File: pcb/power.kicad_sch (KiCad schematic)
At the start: 18 parts, among them J5 9V Battery, J6 9V Barrel Female, U3 MCP1700T-3302E/TT, U4 TPS54302

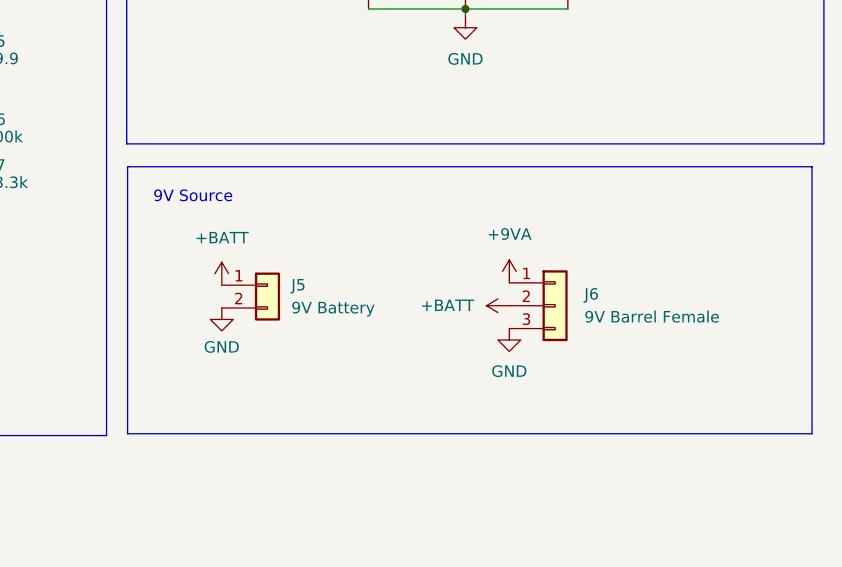
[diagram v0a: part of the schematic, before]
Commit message: Added filtering cap to 9V barrel
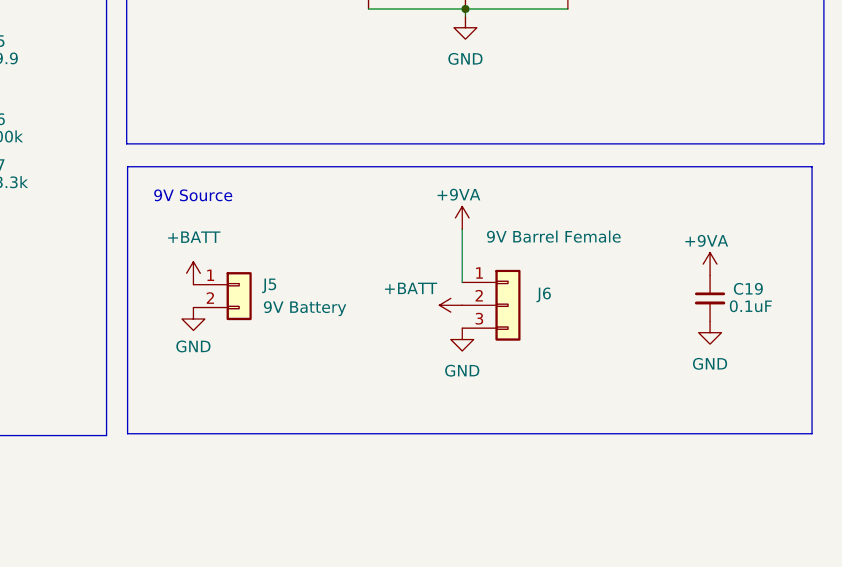
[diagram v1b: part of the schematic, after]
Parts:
- added C19: 0.1uF, symbol Device:C_Small
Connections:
- net +9VA: now also C19.1
- net GND: now also C19.2
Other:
- moved on the sheet: J5, J6

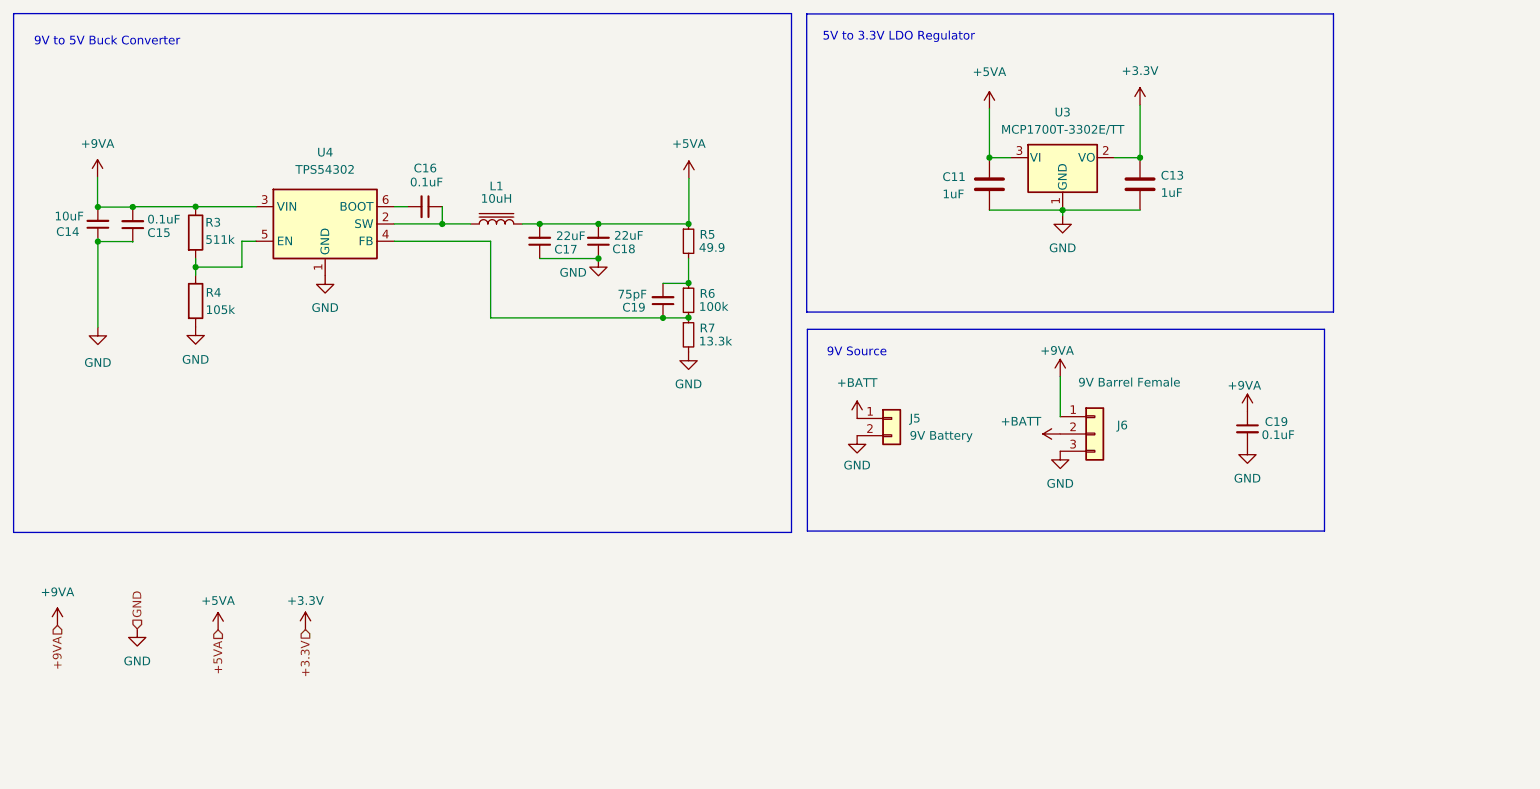
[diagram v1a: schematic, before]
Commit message: Removed power hierarchy labels
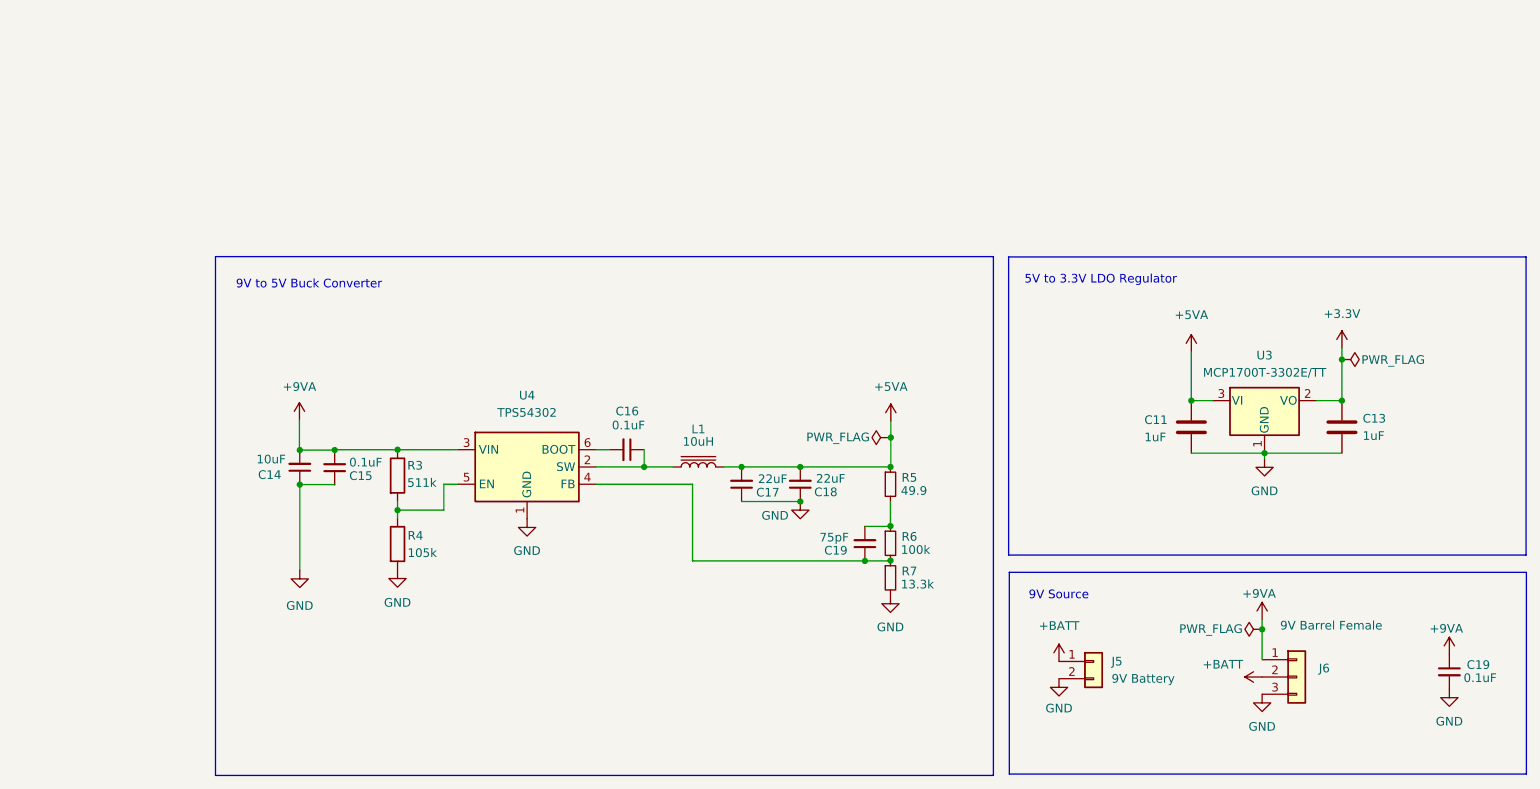
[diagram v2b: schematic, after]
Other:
- moved on the sheet: C11, C13, C14, C15, C16, C17, C18, C19, J5, J6, L1, R3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

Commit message: Reordered components
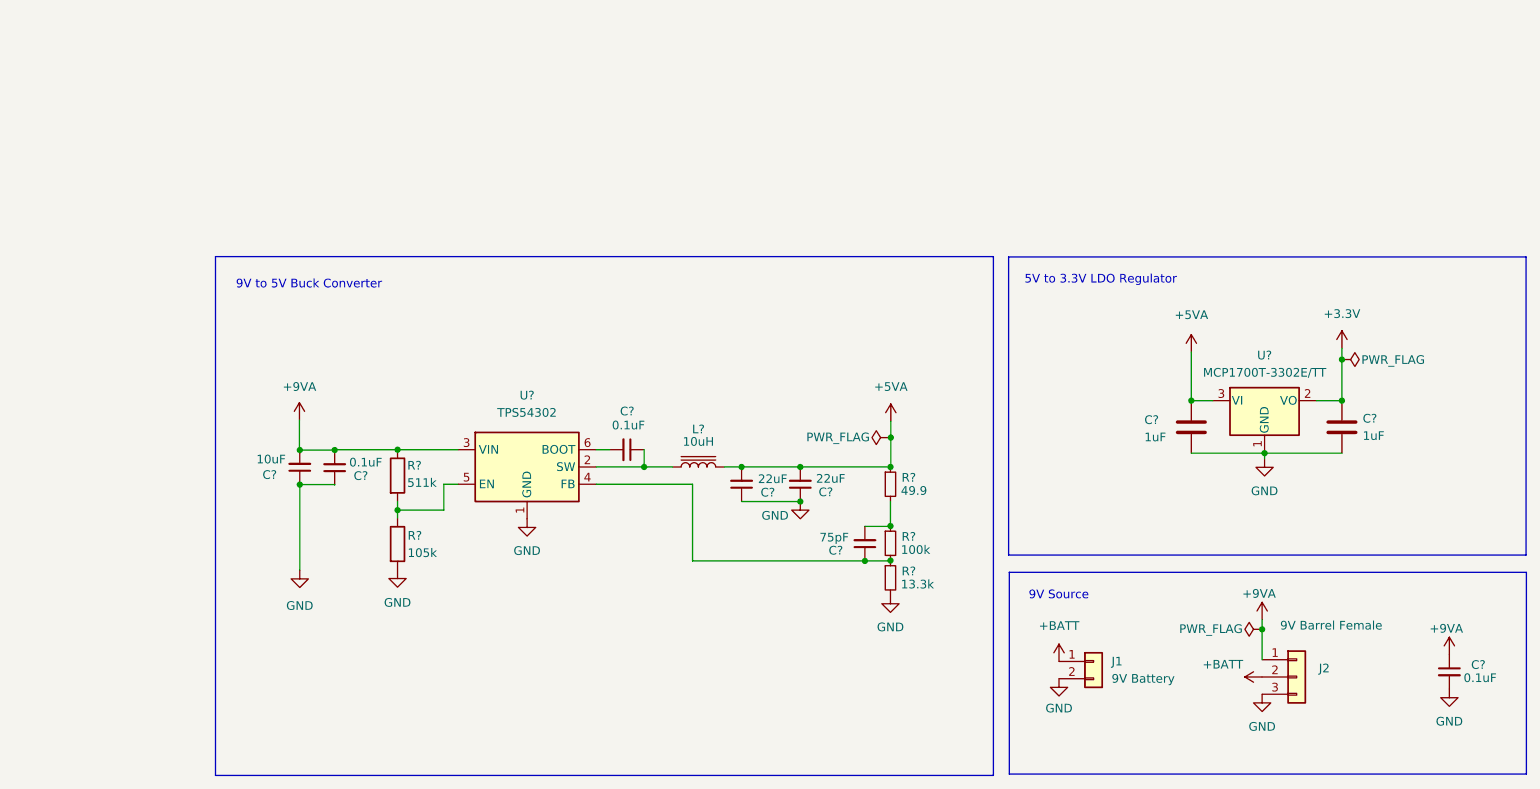
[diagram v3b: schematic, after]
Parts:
- renumbered C19 to C?, C16 to C?, C15 to C?, C13 to C?, C17 to C?, C14 to C?, C11 to C?, C18 to C?, J5 to J1, J6 to J2, L1 to L?, R3 to R?, R7 to R?, R5 to R?, R6 to R?, R4 to R?, U4 to U?, U3 to U?

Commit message: Assigned footprints and jlcpcb part number to all components
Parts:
- C? (x3): footprint (none) -> Capacitor_SMD:C_1206_3216Metric; LCSC (none) -> C577121; MPN (none) -> CC1206JKNPO9BN104; Manufacturer (none) -> Yageo
- C? (x2): footprint (none) -> Capacitor_SMD:C_0805_2012Metric; LCSC (none) -> C1712; MPN (none) -> CL21B105KAFNFNE; Manufacturer (none) -> Samsung Electro-Mechanics
- C? (x2): footprint (none) -> Capacitor_SMD:C_1206_3216Metric; LCSC (none) -> C91604; MPN (none) -> GRM31CR71A226KE15L; Manufacturer (none) -> Murata
- C?: footprint (none) -> Capacitor_Tantalum_SMD:CP_EIA-3216-18_Kemet-A; LCSC (none) -> C7177; MPN (none) -> TAJA106K010RNJ
- C?: footprint (none) -> Capacitor_SMD:C_0402_1005Metric; LCSC (none) -> C107010; MPN (none) -> CC0402JRNPO9BN750; Manufacturer (none) -> Yageo
- L?: footprint (none) -> Inductor_SMD:L_6.3x6.3_H3; LCSC (none) -> C2849537; MPN (none) -> PNLS6045-100M 10UH; Manufacturer (none) -> DMBJ
- R?: footprint (none) -> Resistor_SMD:R_0603_1608Metric; LCSC (none) -> C188257; MPN (none) -> RC0603FR-07511KL; Manufacturer (none) -> Yageo
- R?: footprint (none) -> Resistor_SMD:R_0603_1608Metric; LCSC (none) -> C185373; MPN (none) -> RC0603FR-0713K3L; Manufacturer (none) -> Yageo
- R?: footprint (none) -> Resistor_SMD:R_0603_1608Metric; LCSC (none) -> C114625; MPN (none) -> RC0603FR-0749R9L; Manufacturer (none) -> Yageo
- R?: footprint (none) -> Resistor_SMD:R_0603_1608Metric; LCSC (none) -> C14675; MPN (none) -> RC0603FR-07100KL; Manufacturer (none) -> Yageo
- R?: footprint (none) -> Resistor_SMD:R_0603_1608Metric; LCSC (none) -> C141685; MPN (none) -> RC0603FR-07105KL; Manufacturer (none) -> Yageo
- U?: LCSC (none) -> C311983; MPN (none) -> TPS54302DDCR; Manufacturer (none) -> Texas Instruments
- U?: LCSC (none) -> C39051; MPN (none) -> MCP1700T-3302E/TT; Manufacturer (none) -> Microchip

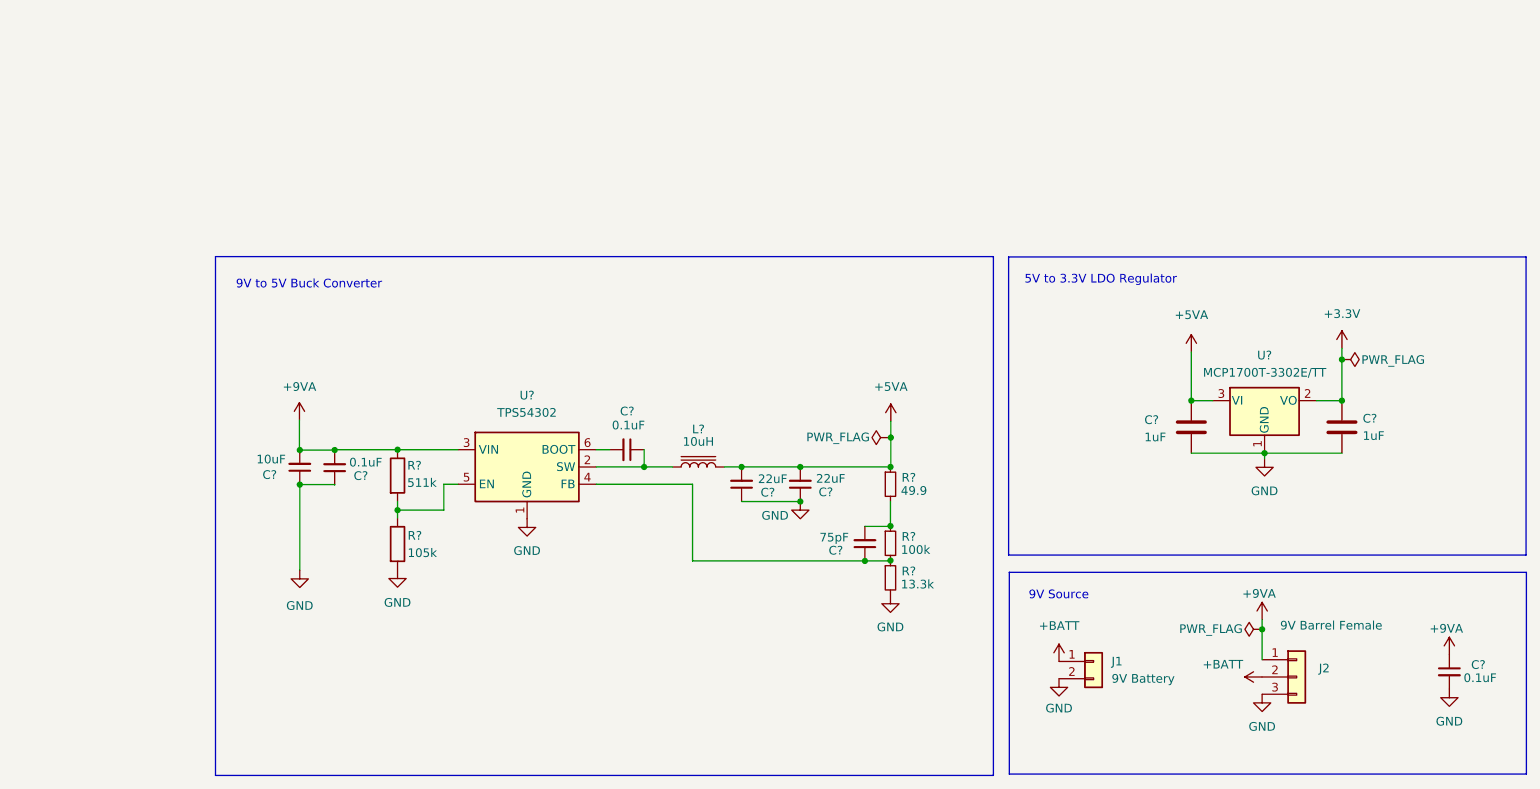
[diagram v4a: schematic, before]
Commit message: Added better filtering for 9V supply
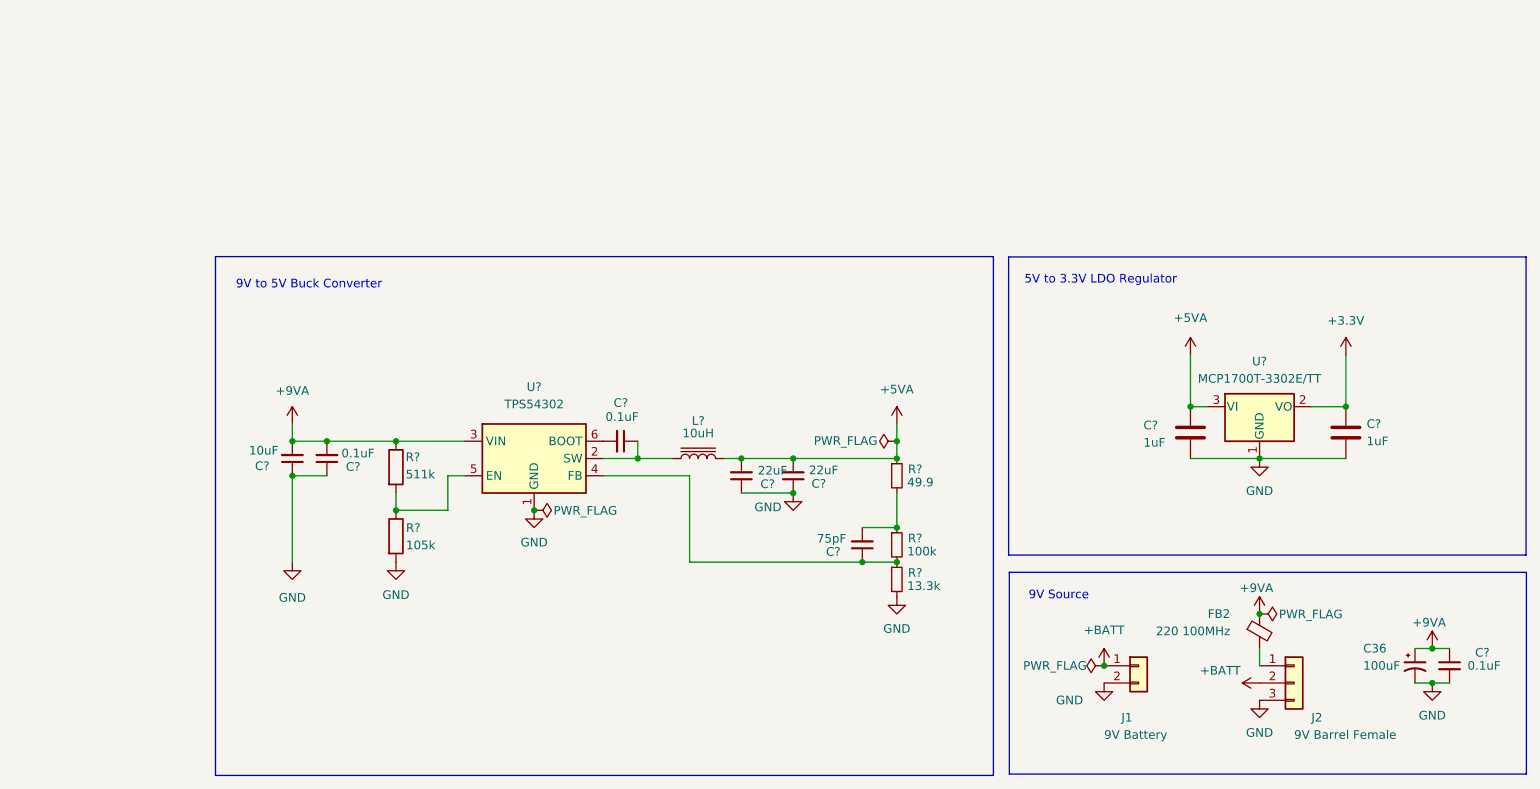
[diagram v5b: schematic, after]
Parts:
- added C36: 100uF, Capacitor_SMD:CP_Elec_6.3x5.4, symbol Device:C_Polarized_Small_US
- added FB2: 220 100MHz, Inductor_SMD:L_0603_1608Metric, symbol Device:FerriteBead_Small
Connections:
- net +9VA: now also C36.1, FB2.1; no longer J2.1 (Pin_1)
- net GND: now also C36.2
- new net: FB2.2, J2.1 (Pin_1)
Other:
- moved on the sheet: C?, J1, J2, L?, R?, U?

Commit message: Starting PCB layout
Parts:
- C?: footprint Capacitor_Tantalum_SMD:CP_EIA-3216-18_Kemet-A -> Capacitor_SMD:C_1206_3216Metric; LCSC C7177 -> C70462; MPN TAJA106K010RNJ -> CC1206KKX7R8BB106; Manufacturer (none) -> Yageo
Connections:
- net +9VA: now also C?.1; no longer C?.2
- net GND: now also C?.2; no longer C?.1
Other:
- moved on the sheet: C?
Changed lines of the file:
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@@
   (junction (at 81.28 83.82) (diameter 0) (color 0 0 0 0)
   )
+  (junction (at 66.04 88.9) (diameter 0) (color 0 0 0 0)
+  )
   (junction (at 132.08 86.36) (diameter 0) (color 0 0 0 0)
   )
@@
   (junction (at 154.94 86.36) (diameter 0) (color 0 0 0 0)
   )
-  (junction (at 66.04 88.9) (diameter 0) (color 0 0 0 0)
-  )
   (junction (at 139.7 86.36) (diameter 0) (color 0 0 0 0)
   )
   (junction (at 81.28 93.98) (diameter 0) (color 0 0 0 0)
   )
+  (junction (at 66.04 83.82) (diameter 0) (color 0 0 0 0)
+  )
   (junction (at 208.28 86.36) (diameter 0) (color 0 0 0 0)
   )
   (junction (at 139.7 91.44) (diameter 0) (color 0 0 0 0)
-  )
-  (junction (at 66.04 83.82) (diameter 0) (color 0 0 0 0)
   )
   (junction (at 154.94 101.6) (diameter 0) (color 0 0 0 0)
@@
     )
   )
-  (symbol (lib_id "Device:C_Small") (at 66.04 86.36 180) (unit 1)
-    (in_bom yes) (on_board yes) (dnp no)
-    (property "Reference" "C?" (at 61.6204 87.4776 0)
-      (effects (font (size 1.27 1.27)))
-    )
-    (property "Value" "10uF" (at 61.8236 85.1916 0)
-      (effects (font (size 1.27 1.27)))
-    )
-    (property "Footprint" "Capacitor_Tantalum_SMD:CP_EIA-3216-18_Kemet-A" (at 66.04 86.36 0)
+  (symbol (lib_id "Device:C_Small") (at 66.04 86.36 0) (unit 1)
+    (in_bom yes) (on_board yes) (dnp no)
+    (property "Reference" "C?" (at 61.5594 85.3849 0)
+      (effects (font (size 1.27 1.27)))
+    )
+    (property "Value" "10uF" (at 61.3562 87.6709 0)
+      (effects (font (size 1.27 1.27)))
+    )
+    (property "Footprint" "Capacitor_SMD:C_1206_3216Metric" (at 66.04 86.36 0)
       (effects (font (size 1.27 1.27)) hide)
     )
@@
       (effects (font (size 1.27 1.27)) hide)
     )
-    (property "LCSC" "C7177" (at 66.04 86.36 0)
-      (effects (font (size 1.27 1.27)) hide)
-    )
-    (property "MPN" "TAJA106K010RNJ" (at 66.04 86.36 0)
-      (effects (font (size 1.27 1.27)) hide)
-    )
+    (property "LCSC" "C70462" (at 66.04 86.36 0)
+      (effects (font (size 1.27 1.27)) hide)
+    )
+    (property "MPN" "CC1206KKX7R8BB106" (at 66.04 86.36 0)
+      (effects (font (size 1.27 1.27)) hide)
+    )
+    (property "Manufacturer" "Yageo" (at 66.04 86.36 0)
+      (effects (font (size 1.27 1.27)) hide)
+    )
